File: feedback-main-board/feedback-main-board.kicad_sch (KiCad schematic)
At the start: 16 parts, among them J1 908140508, J2 FLIP, J3 RPT, Q1 MMFTP3401, U1 OPA1679

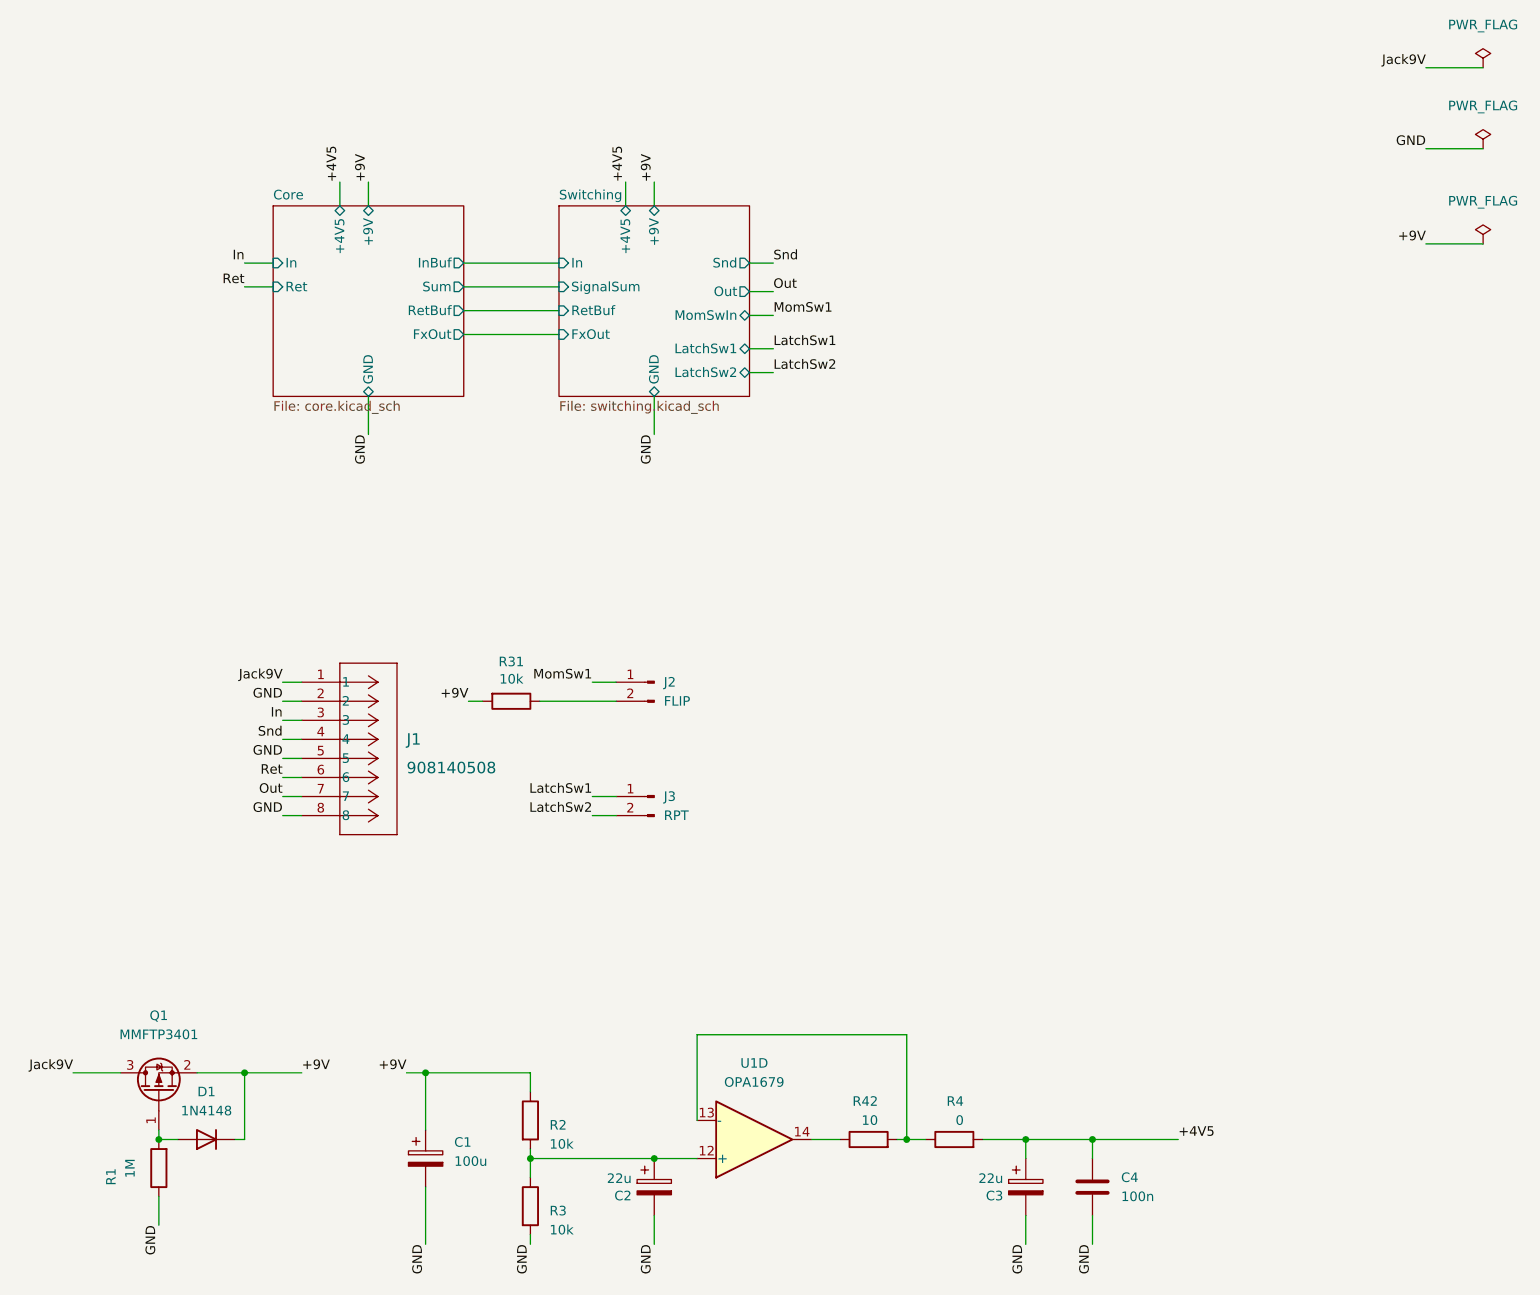
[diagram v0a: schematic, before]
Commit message: JFET switching + reroute + FBD connector
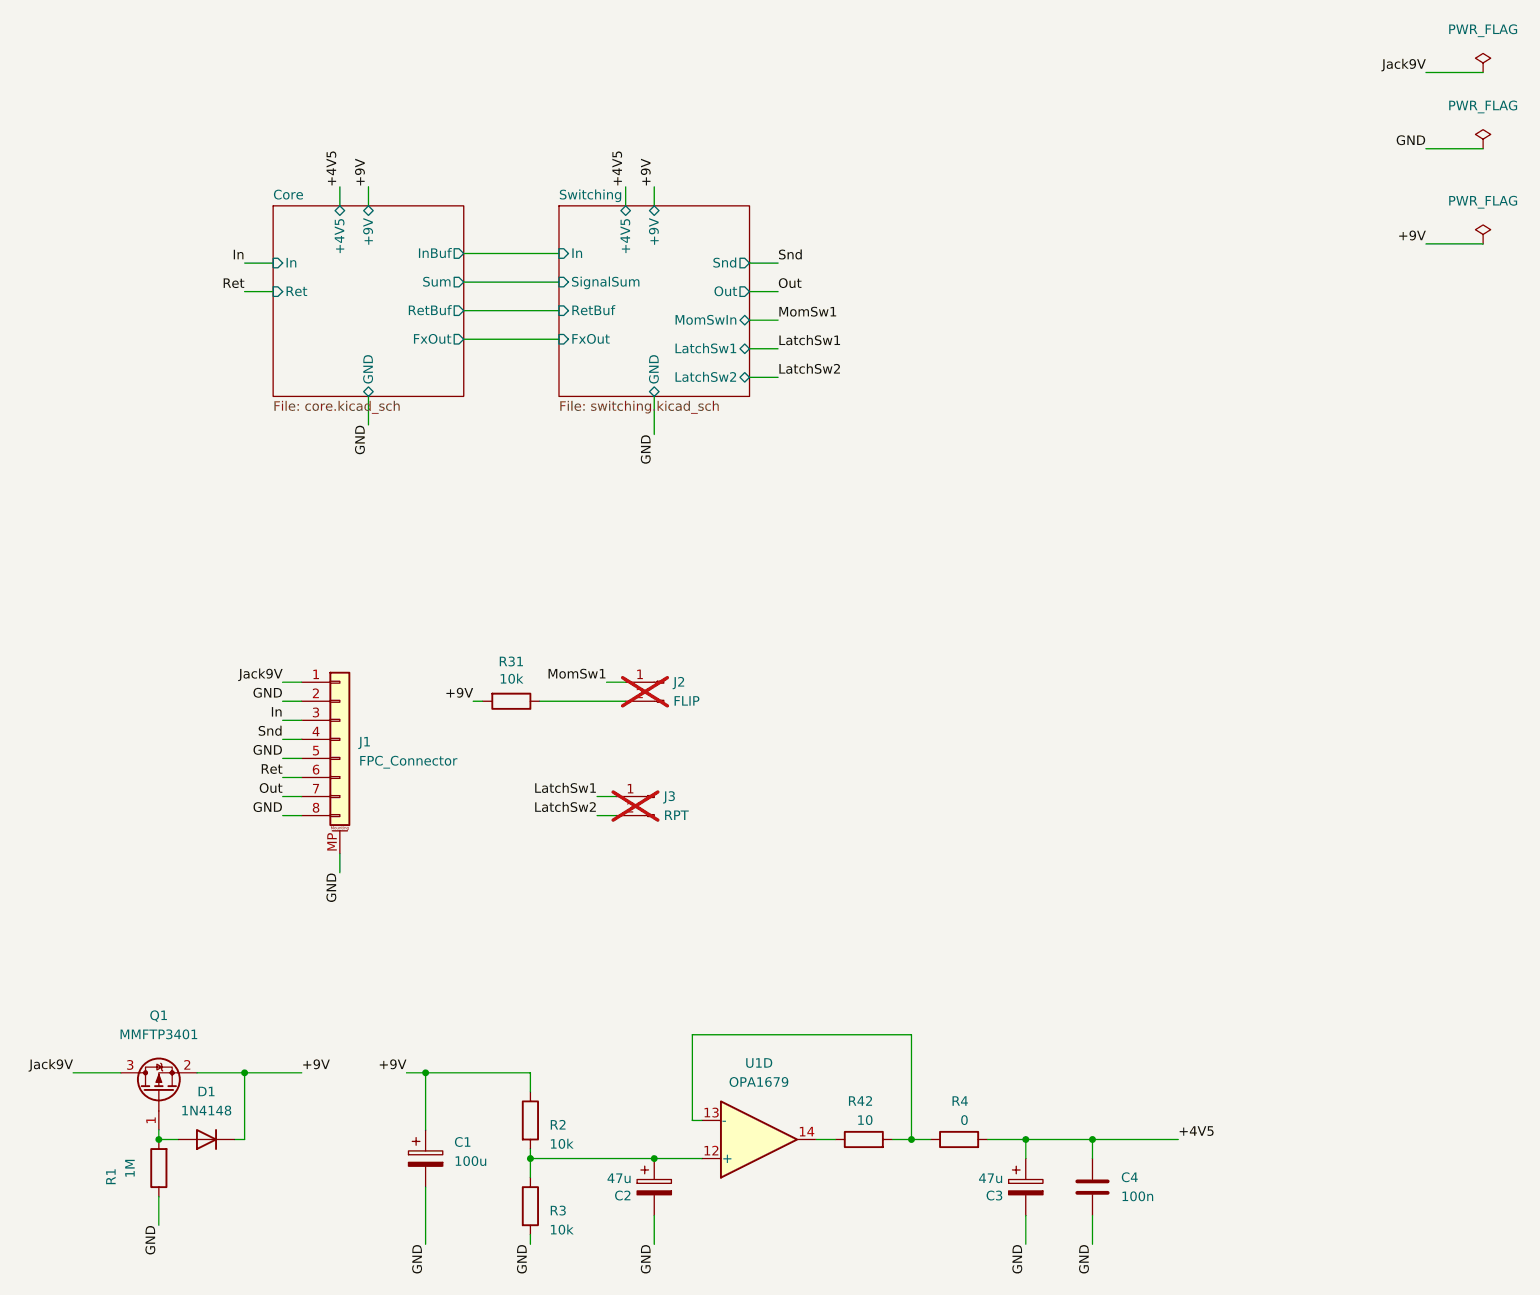
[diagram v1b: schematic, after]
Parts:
- removed J1: 908140508, molex-picoflex8:CONN_SDA-90814_08_MOL, symbol molex-picoflex8:908140508
- added J1: FPC_Connector, Connector_FFC-FPC:JUSHUO_AFA07-S08FCA-00_1x8-1MP_P1.0mm_Horizontal, symbol Connector_Generic_MountingPin:Conn_01x08_MountingPin
- C2, C3: value 22u -> 47u; LCSC C23289 -> C4747958
- D1: LCSC C6423741 -> C2128
- J2, J3: now not fitted
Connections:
- net GND: now also J1.2 (Pin_2), J1.5 (Pin_5), J1.8 (Pin_8), J1.MP (MountPin)
- net In: now also J1.3 (Pin_3)
- net Jack9V: now also J1.1 (Pin_1)
- net Out: now also J1.7 (Pin_7)
- net Ret: now also J1.6 (Pin_6)
- net Snd: now also J1.4 (Pin_4)
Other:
- company: Pedal Markt / Andrei Salomatin -> Andrei Salomatin / akkusativ
- title: Read/Repeat -> RDRPT
- moved on the sheet: R4, R42, U1D
